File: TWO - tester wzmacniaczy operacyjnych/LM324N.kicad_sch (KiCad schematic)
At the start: 3 parts, among them U1 LM324

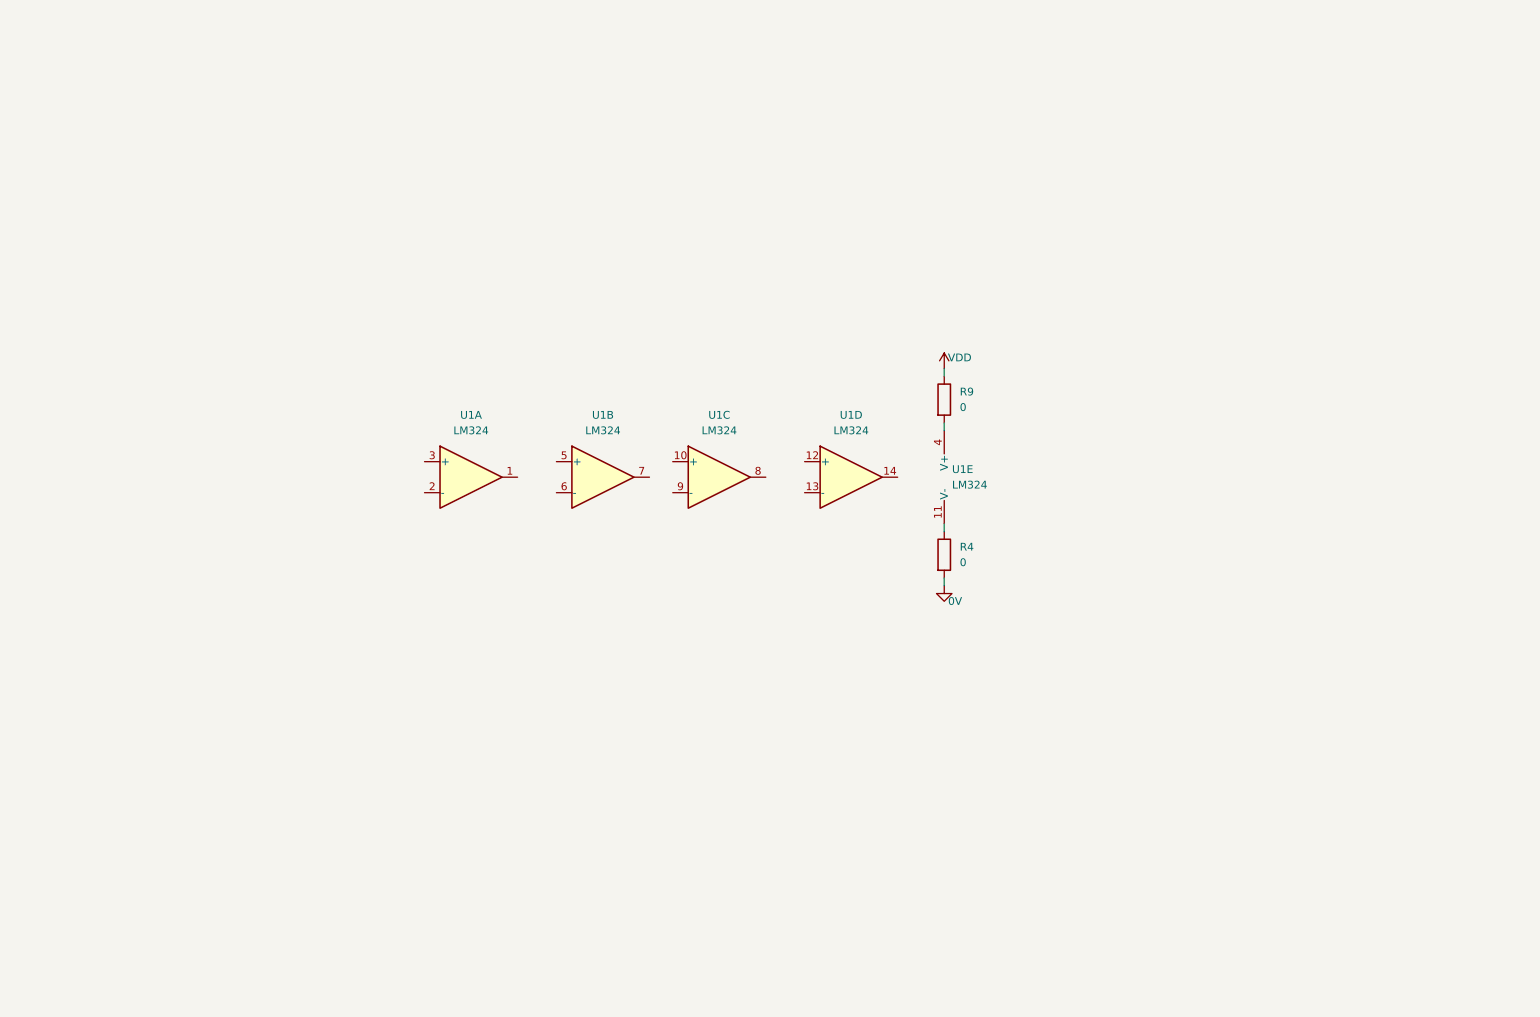
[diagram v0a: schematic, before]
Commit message: Modify LM358N sheet and m324N
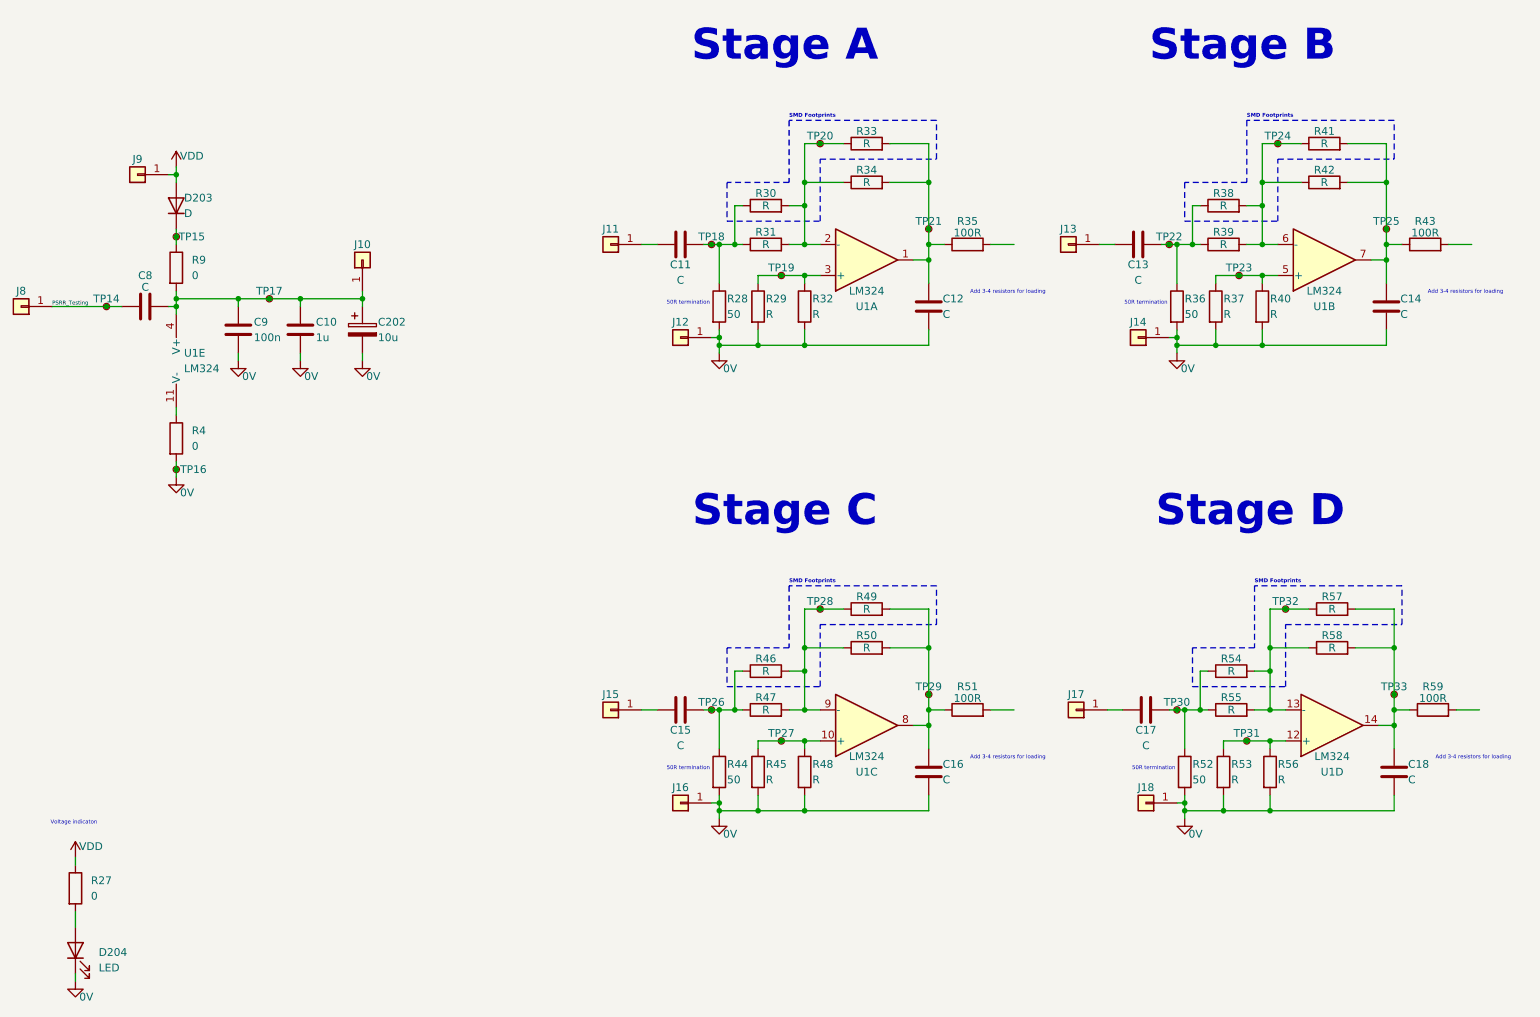
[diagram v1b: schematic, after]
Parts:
- added C10: 1u, Capacitor_THT:C_Disc_D7.5mm_W2.5mm_P5.00mm, symbol Device:C
- added C11, C13, C15, C17: C, Capacitor_THT:C_Disc_D3.8mm_W2.6mm_P2.50mm, symbol Device:C
- added C12, C14, C16, C18, C8: C, symbol Device:C
- added C202: 10u, symbol Device:C_Polarized
- added C9: 100n, Capacitor_THT:C_Disc_D7.5mm_W2.5mm_P5.00mm, symbol Device:C
- added D203: D, symbol Device:D
- added D204: LED, symbol Device:LED
- added J10, J11, J12, J13, J14, J15, J16, J17, J18, J8, J9: Conn_01x01, Connector_PinHeader_2.54mm:PinHeader_1x01_P2.54mm_Vertical, symbol Connector_Generic:Conn_01x01
- added R27: 0, symbol Device:R
- added R28, R36, R44, R52: 50, symbol Device:R
- added R29, R30, R33, R37, R38, R41, R45, R46, R49, R53, R54, R57: R, Resistor_SMD:R_0805_2012Metric, symbol Device:R
- added R31, R32, R34, R39, R40, R42, R47, R48, R50, R55, R56, R58: R, Resistor_THT:R_Axial_DIN0207_L6.3mm_D2.5mm_P10.16mm_Horizontal, symbol Device:R
- added R35, R43, R51, R59: 100R, symbol Device:R
- added TP14, TP15, TP16, TP17, TP18, TP19, TP20, TP21, TP22, TP23, TP24, TP25, TP26, TP27, TP28, TP29, TP30, TP31, TP32, TP33: TestPoint_Small, symbol Connector:TestPoint_Small
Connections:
- net 0V: now also C10.2, C12.1, C14.1, C16.1, C18.1, C202.2, C9.2, D204.1 (K), J12.1 (Pin_1), J14.1 (Pin_1), J16.1 (Pin_1), J18.1 (Pin_1), R28.2, R29.2, R32.2, R36.2, R37.2, R40.2, R44.2, R45.2, R48.2, R52.2, R53.2, R56.2, TP16.1
- net VDD: now also D203.2 (A), J9.1 (Pin_1), R27.1; no longer R9.1
- net at U1.5 (+): now also R37.1, R40.1, TP23.1
- net at U1.6 (-): now also R38.2, R39.2, R41.1, R42.1, TP24.1
- net at U1.7: now also C14.2, R41.2, R42.2, R43.1, TP25.1
- net at U1.12 (+): now also R53.1, R56.1, TP31.1
- net at U1.13 (-): now also R54.2, R55.2, R57.1, R58.1, TP32.1
- net at U1.14: now also C18.2, R57.2, R58.2, R59.1, TP33.1
- net at U1.10 (+): now also R45.1, R48.1, TP27.1
- net at U1.8: now also C16.2, R49.2, R50.2, R51.1, TP29.1
- net at U1.9 (-): now also R46.2, R47.2, R49.1, R50.1, TP28.1
- net at U1.1: now also C12.2, R33.2, R34.2, R35.1, TP21.1
- net at U1.2 (-): now also R30.2, R31.2, R33.1, R34.1, TP20.1
- net at U1.3 (+): now also R29.1, R32.1, TP19.1
- net at R9.2, U1.4 (V+): now also C10.1, C202.1, C8.2, C9.1, J10.1 (Pin_1), TP17.1
- new net: C11.2, R28.1, R30.1, R31.1, TP18.1
- new net: C13.2, R36.1, R38.1, R39.1, TP22.1
- new net: C17.1, J17.1 (Pin_1)
- new net: C11.1, J11.1 (Pin_1)
- new net: C15.2, R44.1, R46.1, R47.1, TP26.1
- new net: D204.2 (A), R27.2
- new net: C17.2, R52.1, R54.1, R55.1, TP30.1
- new net: C15.1, J15.1 (Pin_1)
- new net: C13.1, J13.1 (Pin_1)
- new net: D203.1 (K), R9.1, TP15.1
- new net PSRR_Testing: C8.1, J8.1 (Pin_1), TP14.1
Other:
- note added: "50R termination"
- note added: "Add 3-4 resistors for loading"
- note added: "SMD Footprints"
- note added: "Stage A"
- note added: "Stage B"
- note added: "Stage C"
- note added: "Stage D"
- note added: "Voltage indicaton"
- moved on the sheet: R4, R9, U1A, U1B, U1C, U1D, U1E
